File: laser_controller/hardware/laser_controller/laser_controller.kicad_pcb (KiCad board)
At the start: 2 copper layers, 30 x 109 mm, 129 parts, among them J1 AudioJack2_SwitchT, J14 USB_C_Receptacle_USB2.0, J16 SI-46001-F, J2 AudioJack2_SwitchT, J3 AudioJack2_SwitchT, J4 AudioJack2_SwitchT, J5 AudioJack2_SwitchT, J6 Conn_02x05_Odd_Even, SW2 SW_Push, SW3 SW_Push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

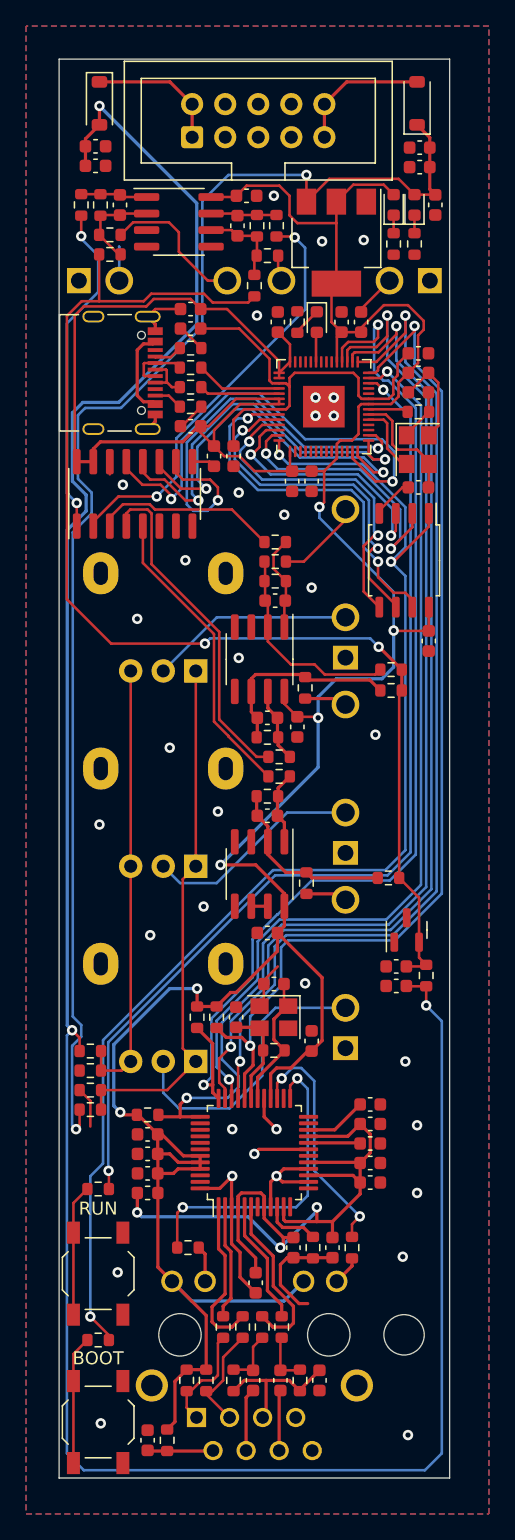
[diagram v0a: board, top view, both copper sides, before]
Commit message: Replaced 3.3V regulator
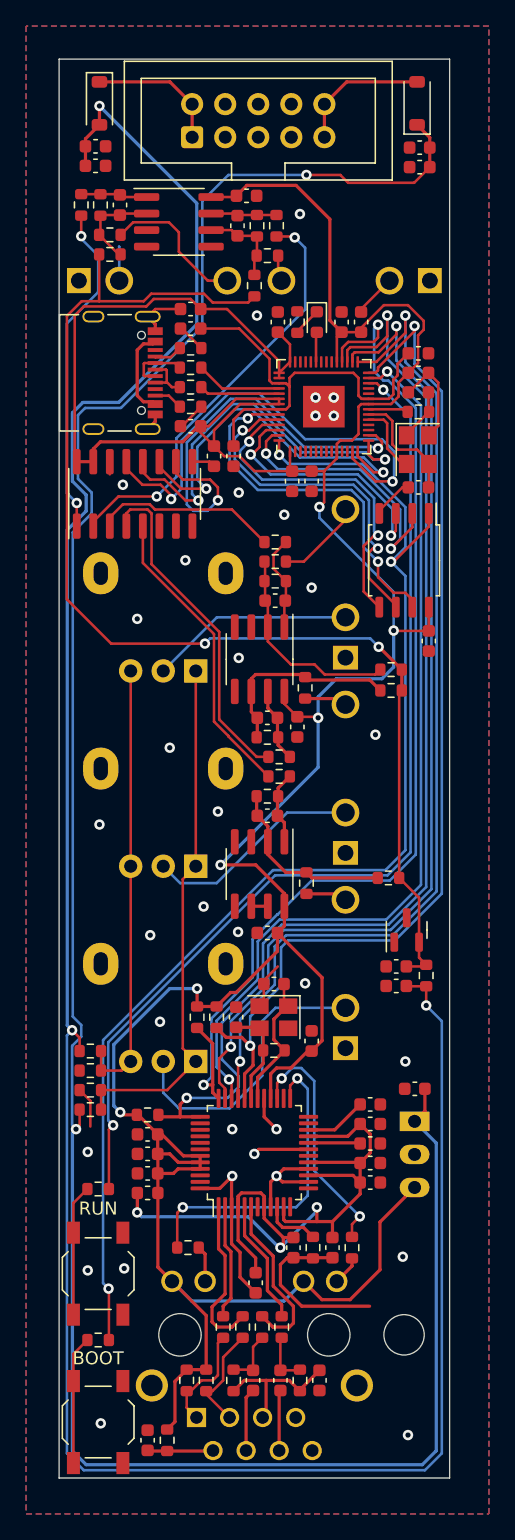
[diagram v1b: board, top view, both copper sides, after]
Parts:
- removed D2, D4: LED, LED_SMD:LED_0603_1608Metric
- removed R79: 4.7k, Resistor_SMD:R_0603_1608Metric
- removed R81: 1k, Resistor_SMD:R_0603_1608Metric
- removed U6: AMS1117-3.3, Package_TO_SOT_SMD:SOT-223-3_TabPin2
- added U10: R-783.3-1.0, Converter_DCDC:Converter_DCDC_RECOM_R-78E-0.5_THT, B.Cu at (66.0, 133.6)
- moved C34 67.9 mm to (66.0, 131.1), turned to 180 degrees
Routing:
- net +12V: track 108.2 -> 185.4 mm
- net +3.3V: track 279.7 -> 286.3 mm
- net GND: track 77.8 -> 82.6 mm
- net Net-(D4-K): track 1.39 -> 0.00 mm
- net Net-(D2-K): track 1.39 -> 0.00 mm
- net /QSPI_SS: track 98.1 -> 97.3 mm
